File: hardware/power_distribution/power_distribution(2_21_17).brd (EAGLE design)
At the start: 92.7 x 101.6 mm, 56 parts, among them Q2 60V/32A/35mΩ, Q3 60V/32A/35mΩ

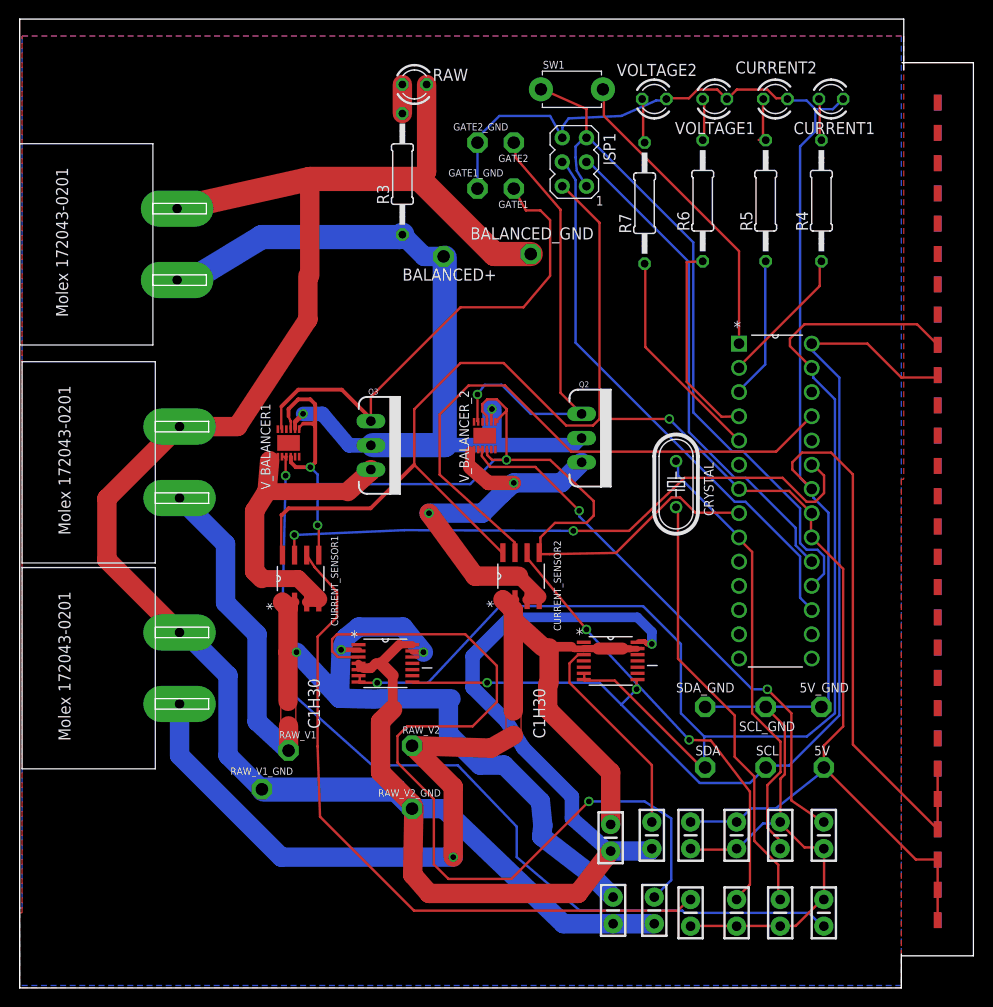
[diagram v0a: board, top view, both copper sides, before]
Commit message: Moved molex connectors to the top and put in silk screen
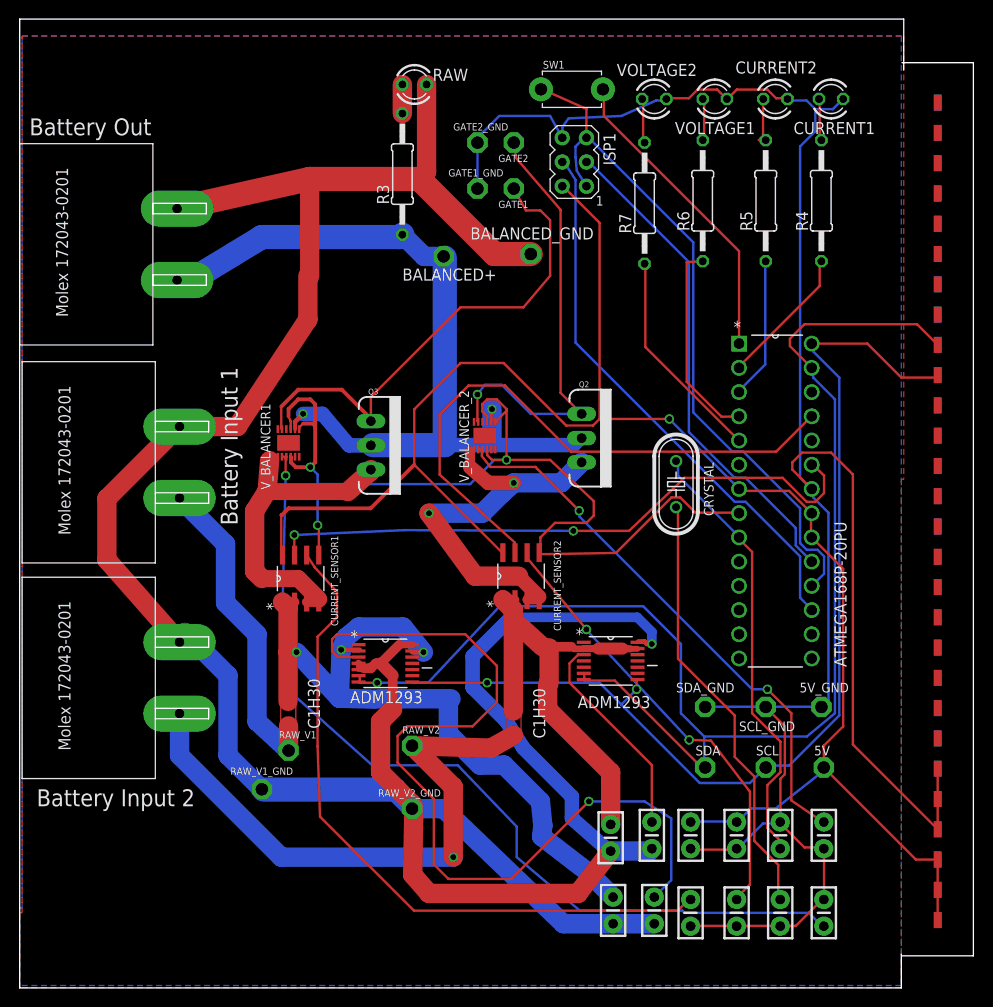
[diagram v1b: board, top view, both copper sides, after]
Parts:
- moved INPUT2 1.02 mm to (14.2, 32.5)
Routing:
- net N$19: track 295.7 -> 297.0 mm
- net N$16: track 63.0 -> 62.0 mm
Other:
- board text added: "Battery Input 1"
- board text added: "Battery Input 2"
- board text added: "Battery Out"
